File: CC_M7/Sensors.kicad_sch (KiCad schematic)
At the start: 11 parts, among them U2 BMI088, U3 BMP388, U4 BMM150, U5 24AA64T-I/OT

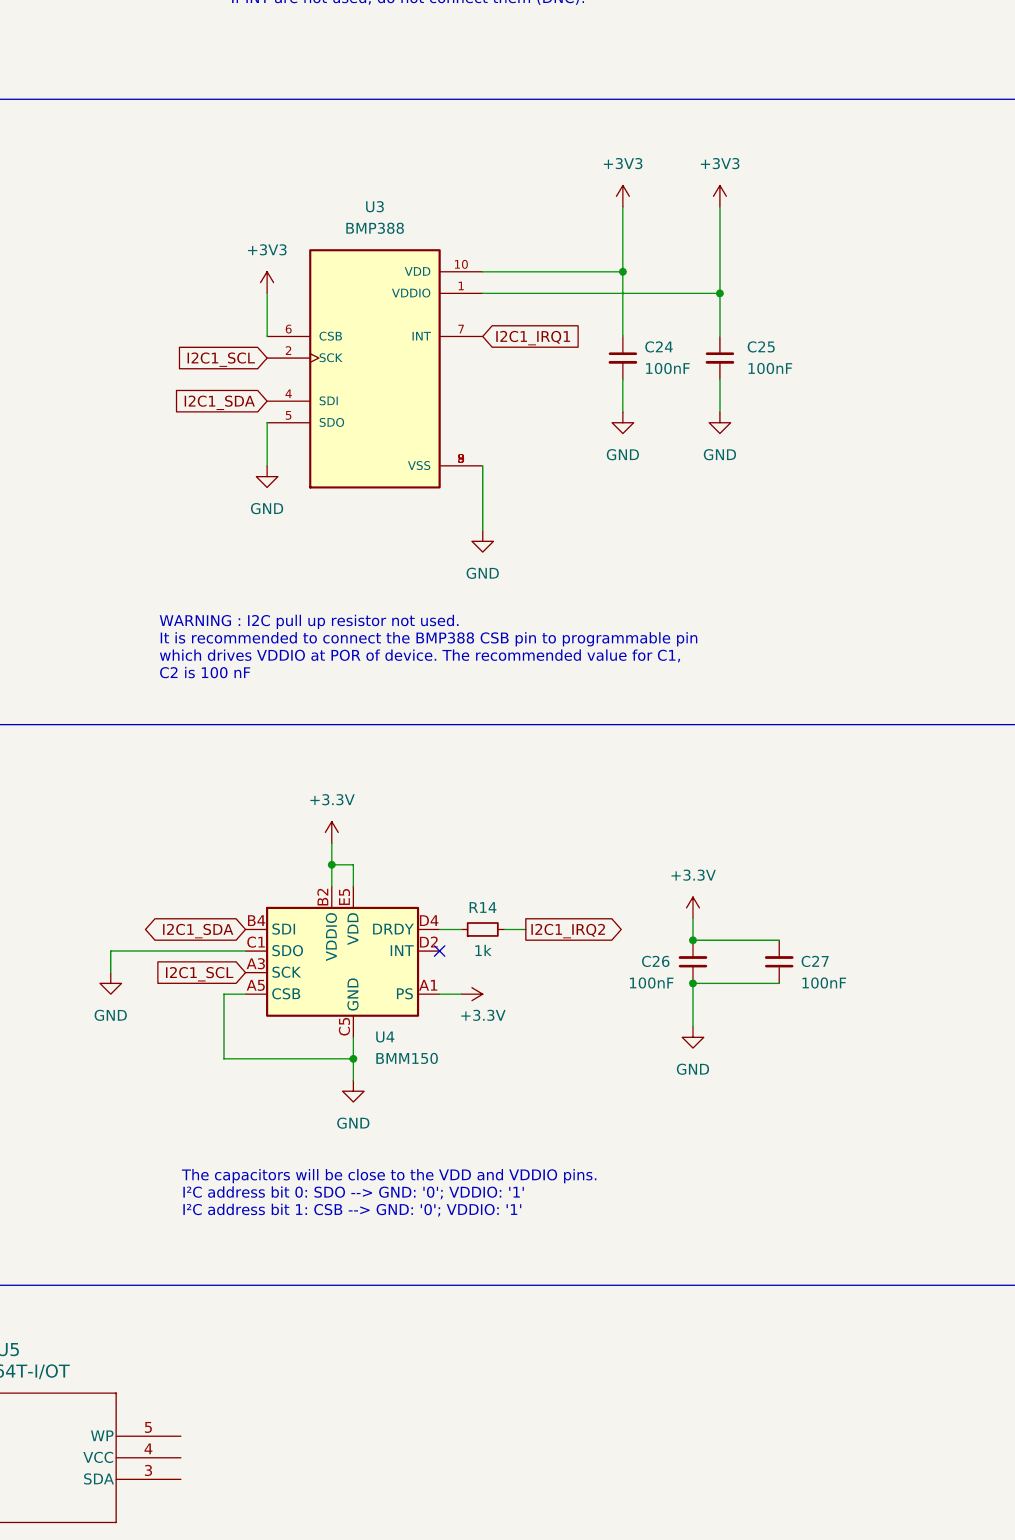
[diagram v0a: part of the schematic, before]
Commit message: NRF pins updated
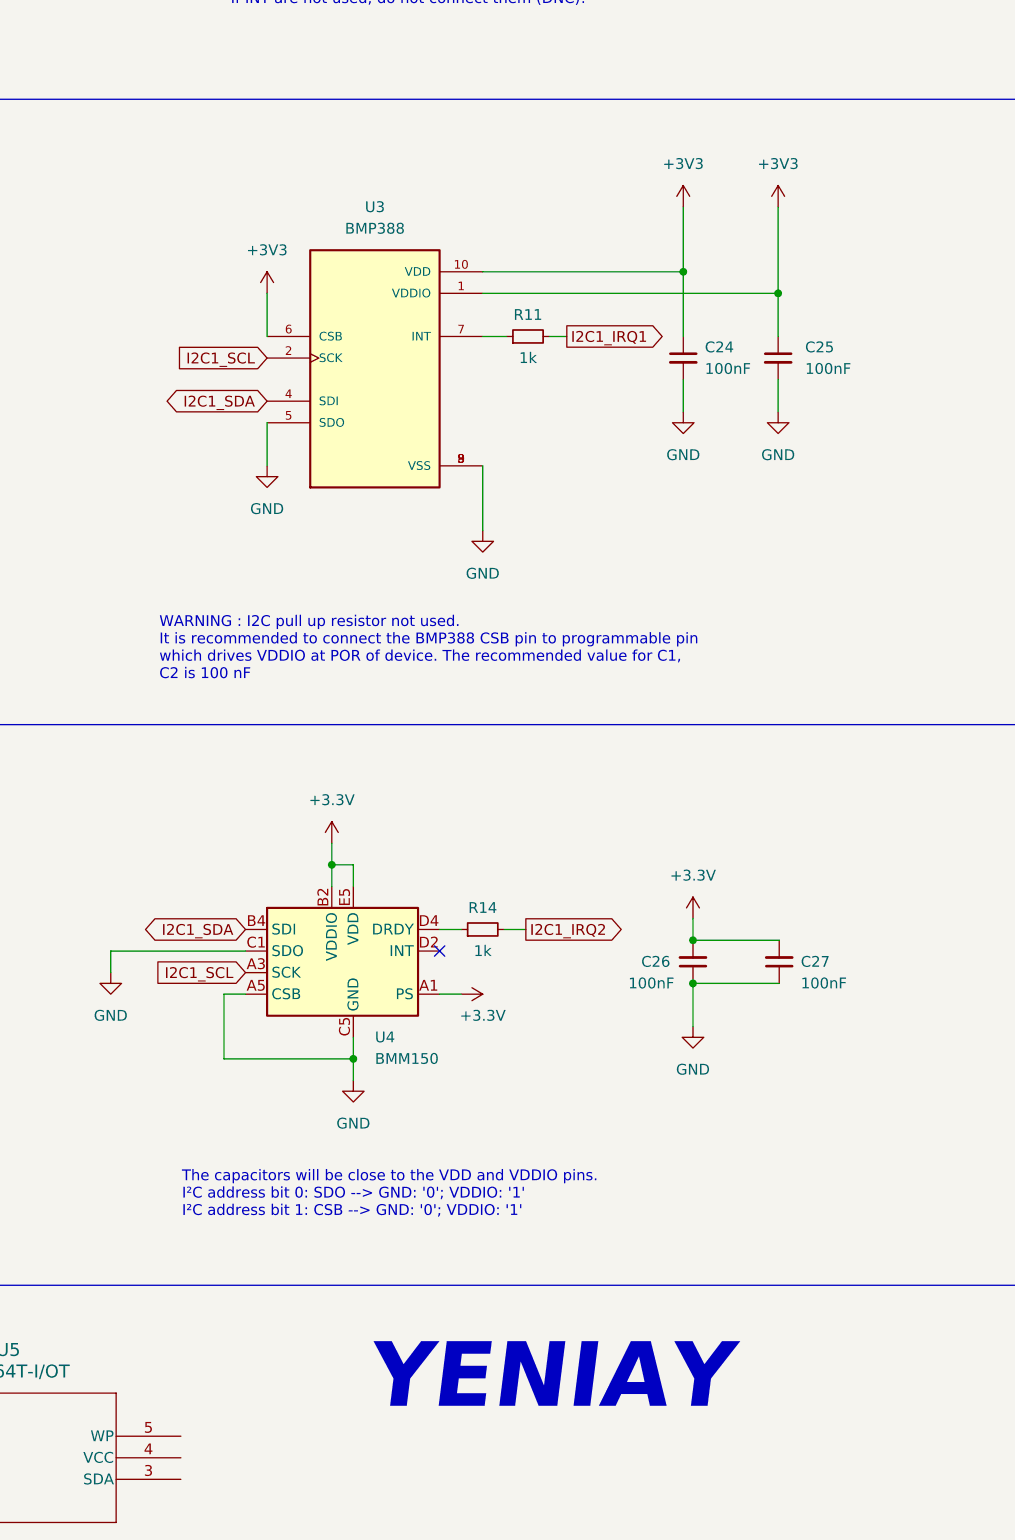
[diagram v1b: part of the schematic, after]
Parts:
- added R11: 1k, symbol Device:R_Small
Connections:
- net I2C1_IRQ1 : no longer names the net of U3.7 (INT)
- net I2C1_IRQ1 : now also R11.1
- net I2C1_SCL  renamed I2C1_SCL
- net I2C1_SDA  renamed I2C1_SDA
- net SPI1_MOSI  renamed SPI1_MOSI
- new net I2C1_IRQ1: R11.2
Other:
- note added: "YENIAY"
- company: YENIAY -> (none)
- moved on the sheet: C24, C25

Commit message: EEPROM
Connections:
- net +3.3V: now also U5.4 (VCC)
- net GND: now also U5.2 (VSS), U5.5 (WP)
- net I2C1_SCL: now also U5.1 (SCL)
- net I2C1_SDA: now also U5.3 (SDA)
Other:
- note added: "EEPROM"
- moved on the sheet: C22, C23, C24, C25, C26, C27, R11, R14, U2, U3, U4, U5

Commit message: final schematic 6 warning
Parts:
- U2: DESCRIPTION Accelerometer, Gyroscope, 6 Axis Sensor I²C, SPI Output -> (none); Description_1 Accelerometer, Gyroscope, 6 Axis Sensor I2C, SPI Output -> Accelerometer, Gyroscope, 6 Axis Sensor I2C, SPI Output
- U3: Purchase-URL (none) -> https://www.snapeda.com/api/url_track_click_mouser/?unipart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
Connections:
- net +3V3 is gone; now on net +3.3V: C22.1, C23.1, C24.1, C25.1, U2.11 (VDDIO), U2.3 (VDD), U3.1 (VDDIO), U3.10 (VDD), U3.6 (CSB)
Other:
- moved on the sheet: C22, C23, C24, C25, R11, U5

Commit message: Changes updated @ CCM7.docx
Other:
- note added: "I2C adresleri yazılacak"
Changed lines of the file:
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@@
+		)
+	)
+	(rectangle
+		(start 12.7 12.7)
+		(end 87.63 29.21)
+		(stroke
+			(width 0)
+			(type default)
+		)
+		(fill
+			(type none)
 		)
 	)
@@
 		)
 	)
+	(text "I2C adresleri yazılacak"
+		(exclude_from_sim no)
+		(at 48.26 20.32 0)
+		(effects
+			(font
+				(size 3.81 3.81)
+				(thickness 0.508)
+				(bold yes)
+			)
+		)
+	)

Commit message: Footprint assignment 1/2
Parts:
- C22, C23, C24, C25, C26, C27: footprint (none) -> Capacitor_SMD:C_0402_1005Metric
- U5: footprint SOT-23-5_MC_MCH -> (none)
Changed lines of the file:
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@@
 			)
 		)
-		(property "Footprint" ""
+		(property "Footprint" "Capacitor_SMD:C_0402_1005Metric"
 			(at 152.4 41.91 0)
 			(effects
@@
 			)
 		)
-		(property "Footprint" ""
+		(property "Footprint" "Capacitor_SMD:C_0402_1005Metric"
 			(at 142.24 41.91 0)
 			(effects
@@
 			)
 		)
-		(property "Footprint" "SOT-23-5_MC_MCH"
+		(property "Footprint" ""
 			(at 27.94 254.508 0)
 			(effects
@@
 			)
 		)
-		(property "Footprint" ""
+		(property "Footprint" "Capacitor_SMD:C_0402_1005Metric"
 			(at 128.27 195.58 0)
 			(effects
@@
 			)
 		)
-		(property "Footprint" ""
+		(property "Footprint" "Capacitor_SMD:C_0402_1005Metric"
 			(at 140.97 127 0)
 			(effects
@@
 			)
 		)
-		(property "Footprint" ""
+		(property "Footprint" "Capacitor_SMD:C_0402_1005Metric"
 			(at 138.43 195.58 0)
 			(effects
@@
 			)
 		)
-		(property "Footprint" ""
+		(property "Footprint" "Capacitor_SMD:C_0402_1005Metric"
 			(at 129.54 127 0)
 			(effects

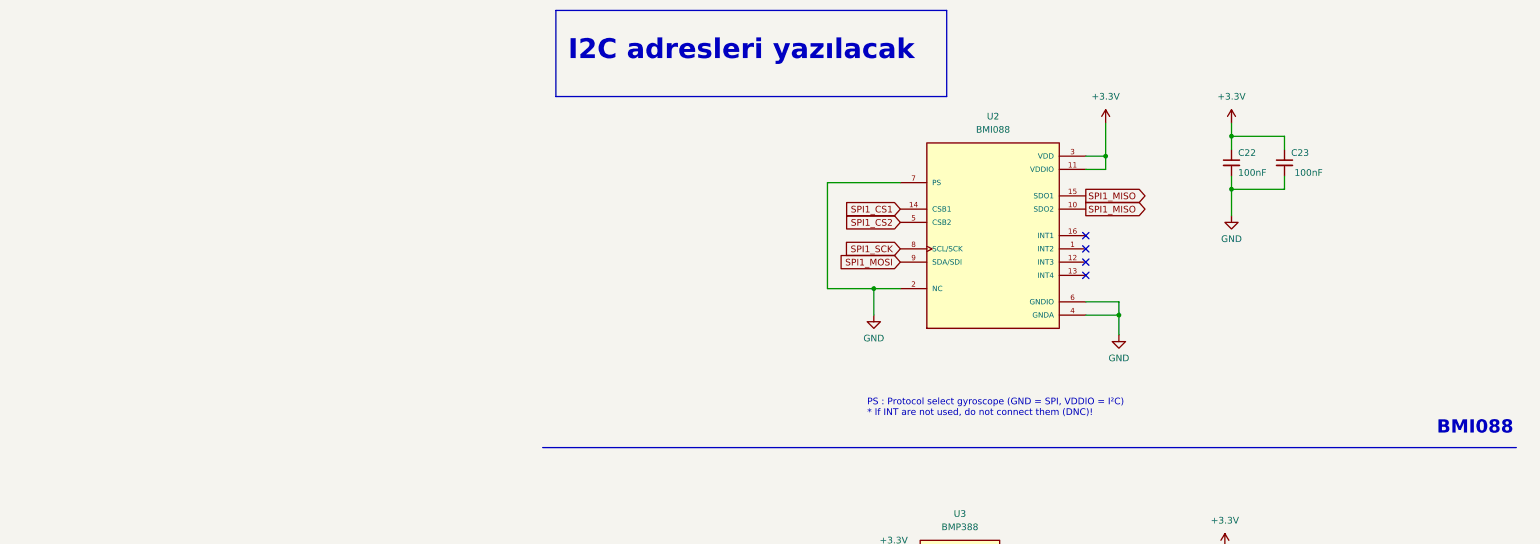
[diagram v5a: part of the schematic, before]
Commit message: IIM42652 schematic added
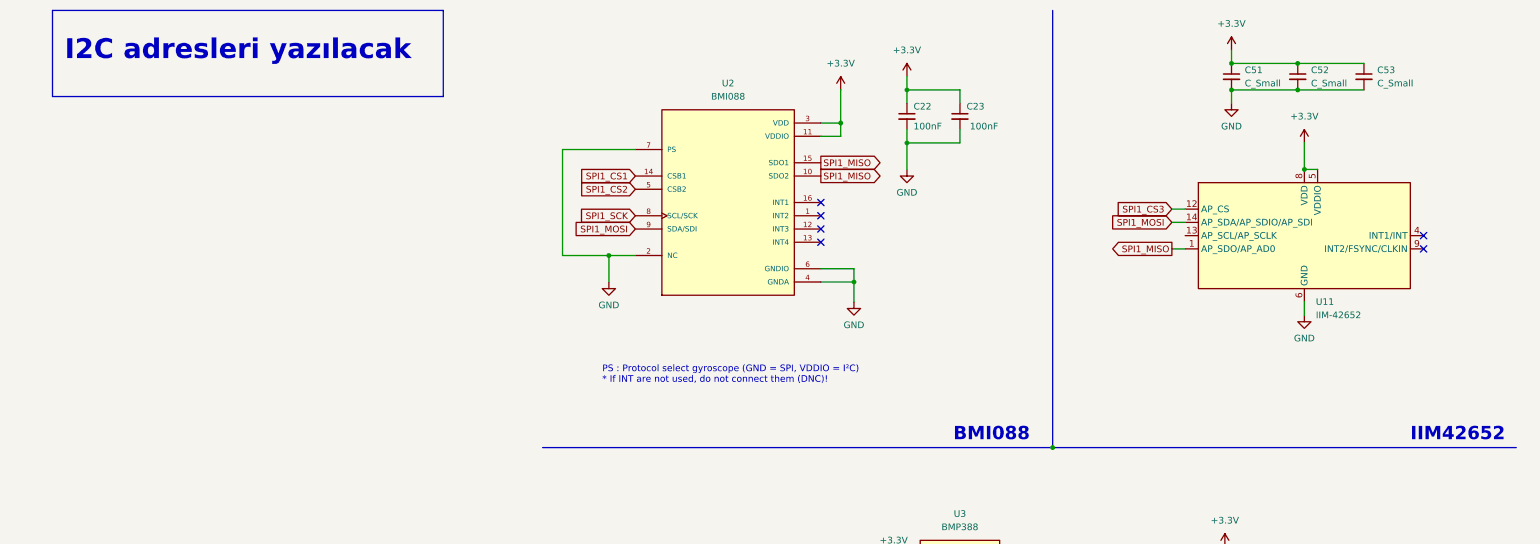
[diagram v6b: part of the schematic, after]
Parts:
- added C51, C52, C53: C_Small, symbol Device:C_Small
- added U11: IIM-42652, Package_LGA:Bosch_LGA-14_3x2.5mm_P0.5mm, symbol Sensor_Motion:IIM-42652
- C22, C23, C24, C25, C26, C27: footprint Capacitor_SMD:C_0402_1005Metric -> Capacitor_SMD:C_0603_1608Metric
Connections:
- net +3.3V: now also C51.1, C52.1, C53.1, U11.5 (VDDIO), U11.8 (VDD)
- net GND: now also C51.2, C52.2, C53.2, U11.6 (GND), U11.7 (GND)
- net SPI1_MISO: now also U11.1 (AP_SDO/AP_AD0)
- net SPI1_MOSI: now also U11.14 (AP_SDA/AP_SDIO/AP_SDI)
- new net SPI1_CS3: U11.12 (AP_CS)
- no-connect marks 5 -> 7
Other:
- note added: "IIM42652"
- moved on the sheet: C22, C23, U2

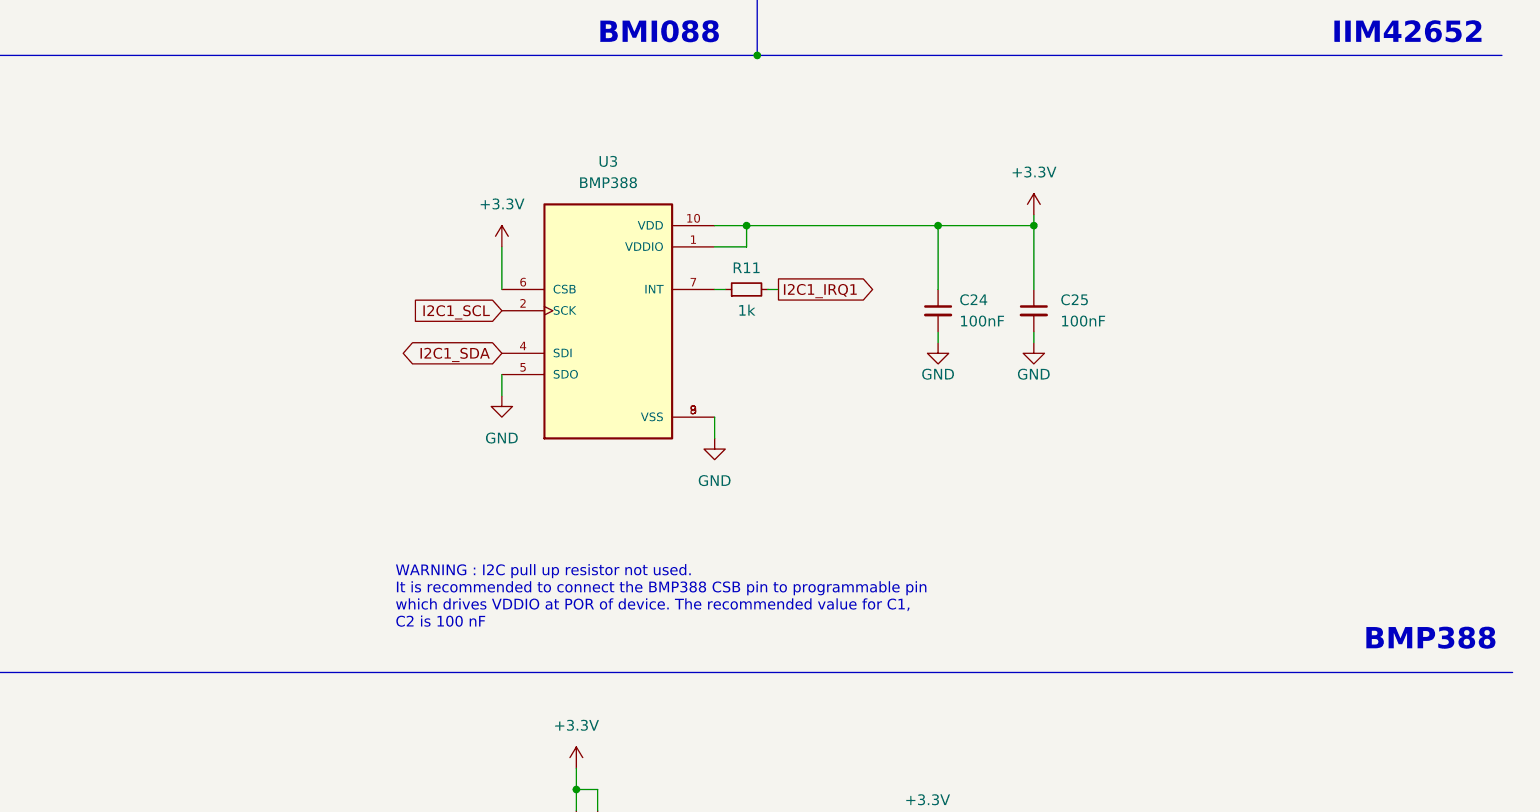
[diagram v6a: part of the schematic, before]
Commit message: BMP581 added schematic
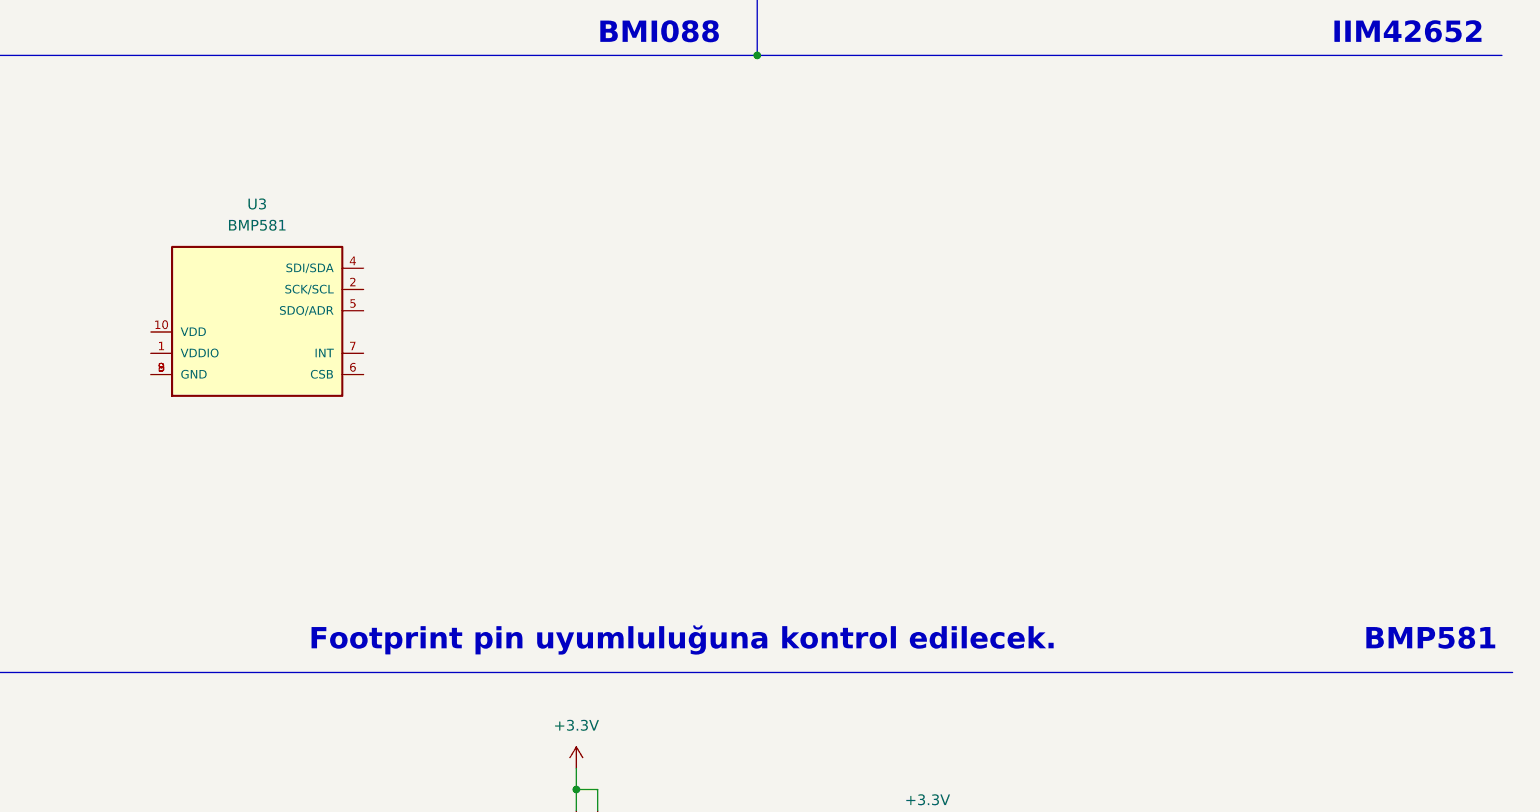
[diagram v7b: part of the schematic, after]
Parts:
- removed C24, C25: 100nF, Capacitor_SMD:C_0603_1608Metric, symbol Device:C_Small
- removed R11: 1k, symbol Device:R_Small
- removed U3: BMP388, BMP388:PQFN50P200X200X80-10N, symbol BMP388:BMP388
- added U3: BMP581, BMP581:BMP581, symbol BMP581:BMP581
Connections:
- new net: U3.3 (GND), U3.8 (GND), U3.9 (GND)
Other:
- note added: "BMP581"
- note added: "Footprint pin uyumluluğuna kontrol edilecek."
- note removed: "BMP388"
- note removed: "WARNING : I2C pull up resistor not used. It is recommended to connect the BMP388 CSB pin to programmable pin which drives VDDIO at POR of device. The recommended value for C1, C2 is 100 nF"
